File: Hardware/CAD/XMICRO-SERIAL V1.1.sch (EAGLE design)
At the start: 92 parts, among them J1 D9-MPH, J2 D9-MPH, J3 MINI-DIN6, J4 PINHD1X3, J5 PINHD1X3, Q1 2N5088, Q2 2N5088, Q3 2N5088, U1 555, U10 74280, U11 74273, U12 74164, U13 74164, U14 7474, U15 74244, U16 74244, U17 74240, U18 74280, U19 74165, U2 7486, U20 74165, U21 74244, U22 7404, U23 74245, U24 16550, U25 16550, U26 75185, U27 75185, U3 7410, U4 7404, U5 7474, U6 7474, U7 7408, U8 74138, U9 74138, Y1 1.8432MHz

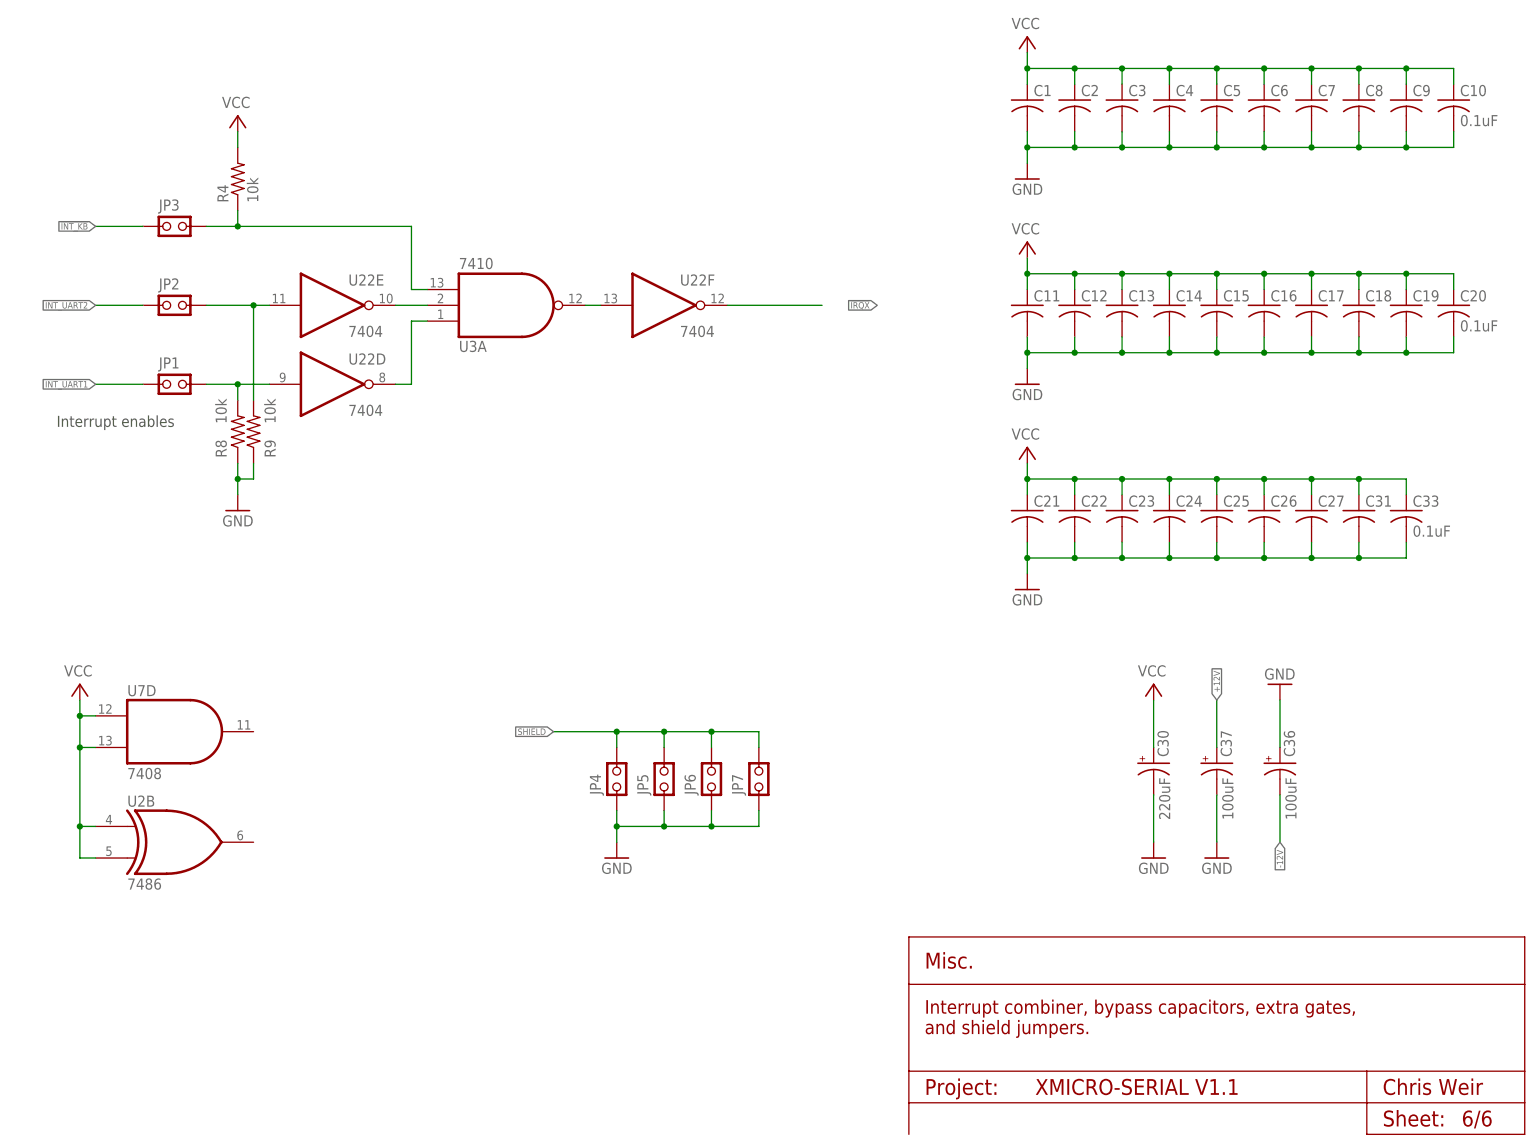
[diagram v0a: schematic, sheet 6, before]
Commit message: Updated design to V1.1 - added Schmitt trigger inputs, improved connector spacing, fixed PS/2 connector footprint
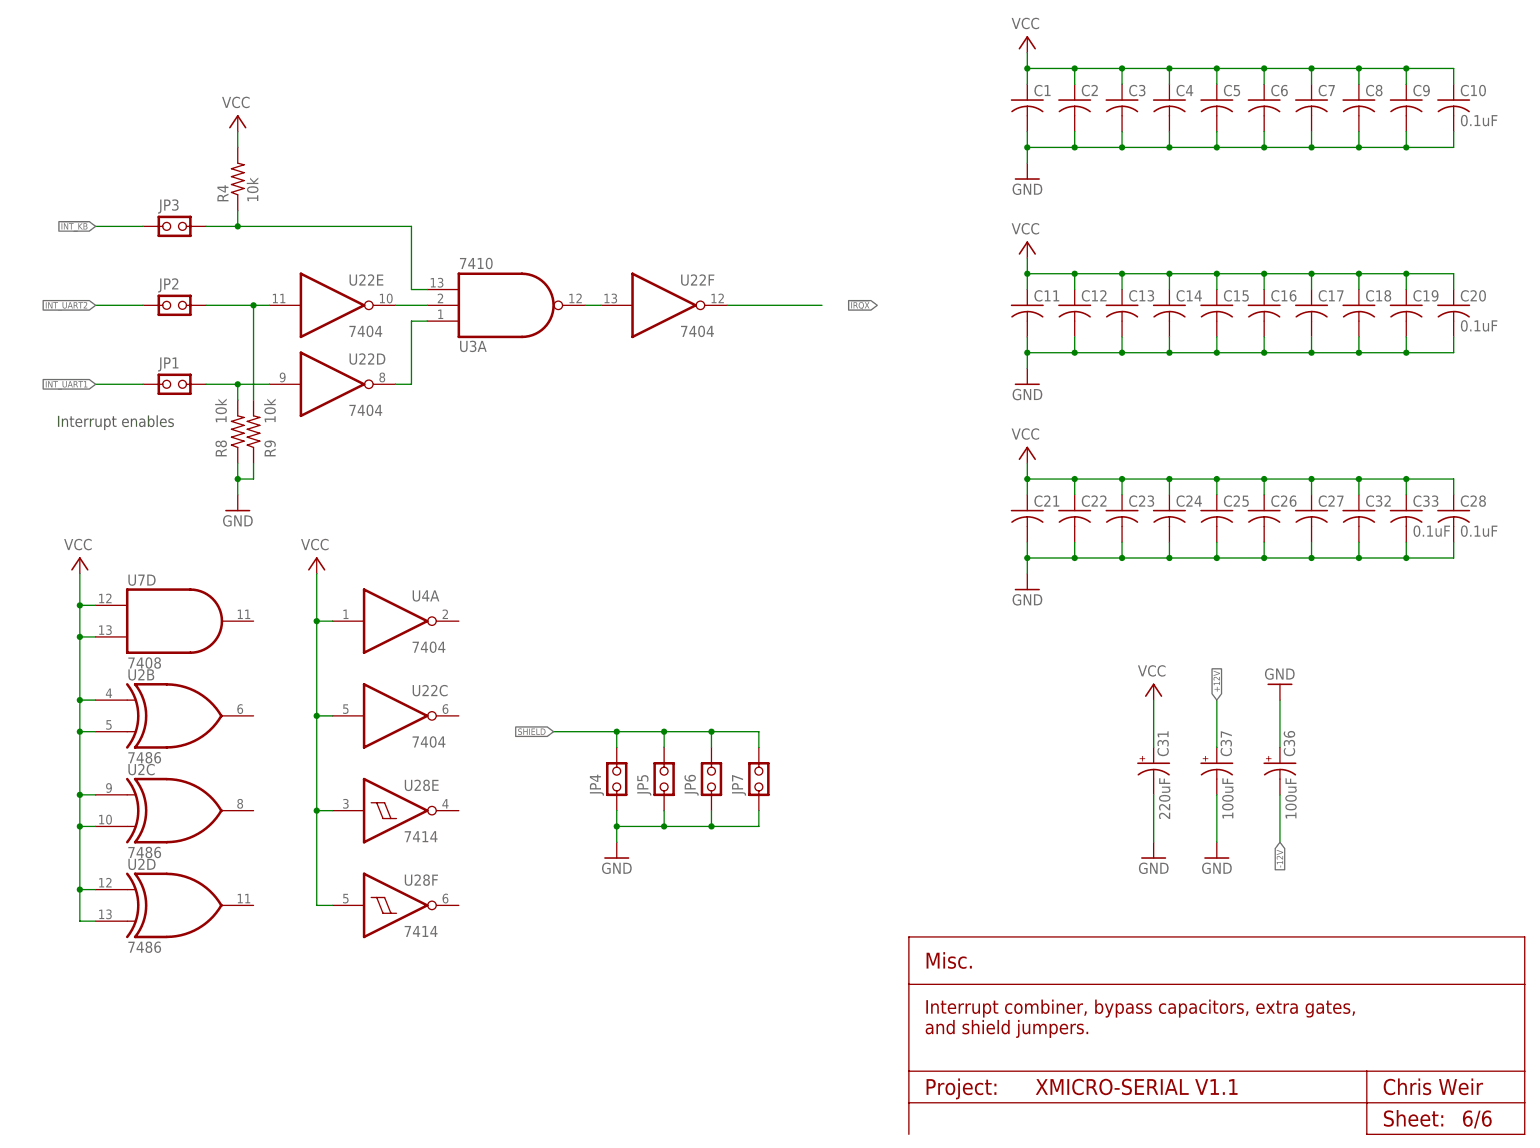
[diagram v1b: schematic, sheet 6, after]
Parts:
- added C32: 0.1uF, Custom:C-US100
- added U28: 7414, 74xx-us:74LS14N
- C28: value 10nF -> 0.1uF
- C29: value 0.1uF -> 10nF; device rcl:CPOL-USE2.5-6 -> Custom:C-US100
- C30: value 220uF -> 0.1uF; device Custom:CPOL-US-10-5 -> rcl:CPOL-USE2.5-6
- C31: value 0.1uF -> 220uF; device Custom:C-US100 -> Custom:CPOL-US-10-5
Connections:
- removed net N$26: U22C.O, U24G$1.RESET, U25G$1.RESET
- new net RST: U24G$1.RESET, U25G$1.RESET, U28C.O, U28D.I
- net !BRST: now also U28C.I; no longer U2D.I1
- net !KB_DATA: now also U28A.O; no longer U4A.O
- net !RST: now also U28D.O; no longer U22C.I, U2D.O
- net BUFF_KB_CLOCK: now also U28B.O; no longer U2C.O
- net GND: now also C29.2, C31.-, C32.2, U8P.GND; no longer C29.-, C31.2, U2C.I1, U2D.I0
- net KB_CLOCK: now also U28B.I; no longer U2C.I0
- net KB_DATA: now also U28A.I; no longer U4A.I
- net N$133: now also C30.+; no longer C29.+
- net N$140: now also C29.1; no longer C28.1
- net VCC: now also C28.1, C31.+, C32.1, U22C.I, U28E.I, U28F.I, U2C.I0, U2C.I1, U2D.I0, U2D.I1, U4A.I, U8P.VCC; no longer C30.+, C31.1
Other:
- moved on the sheet: U2B, U7D

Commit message: Fixed a schematic issue - added second inverter to BUFF_KB_CLOCK signal.
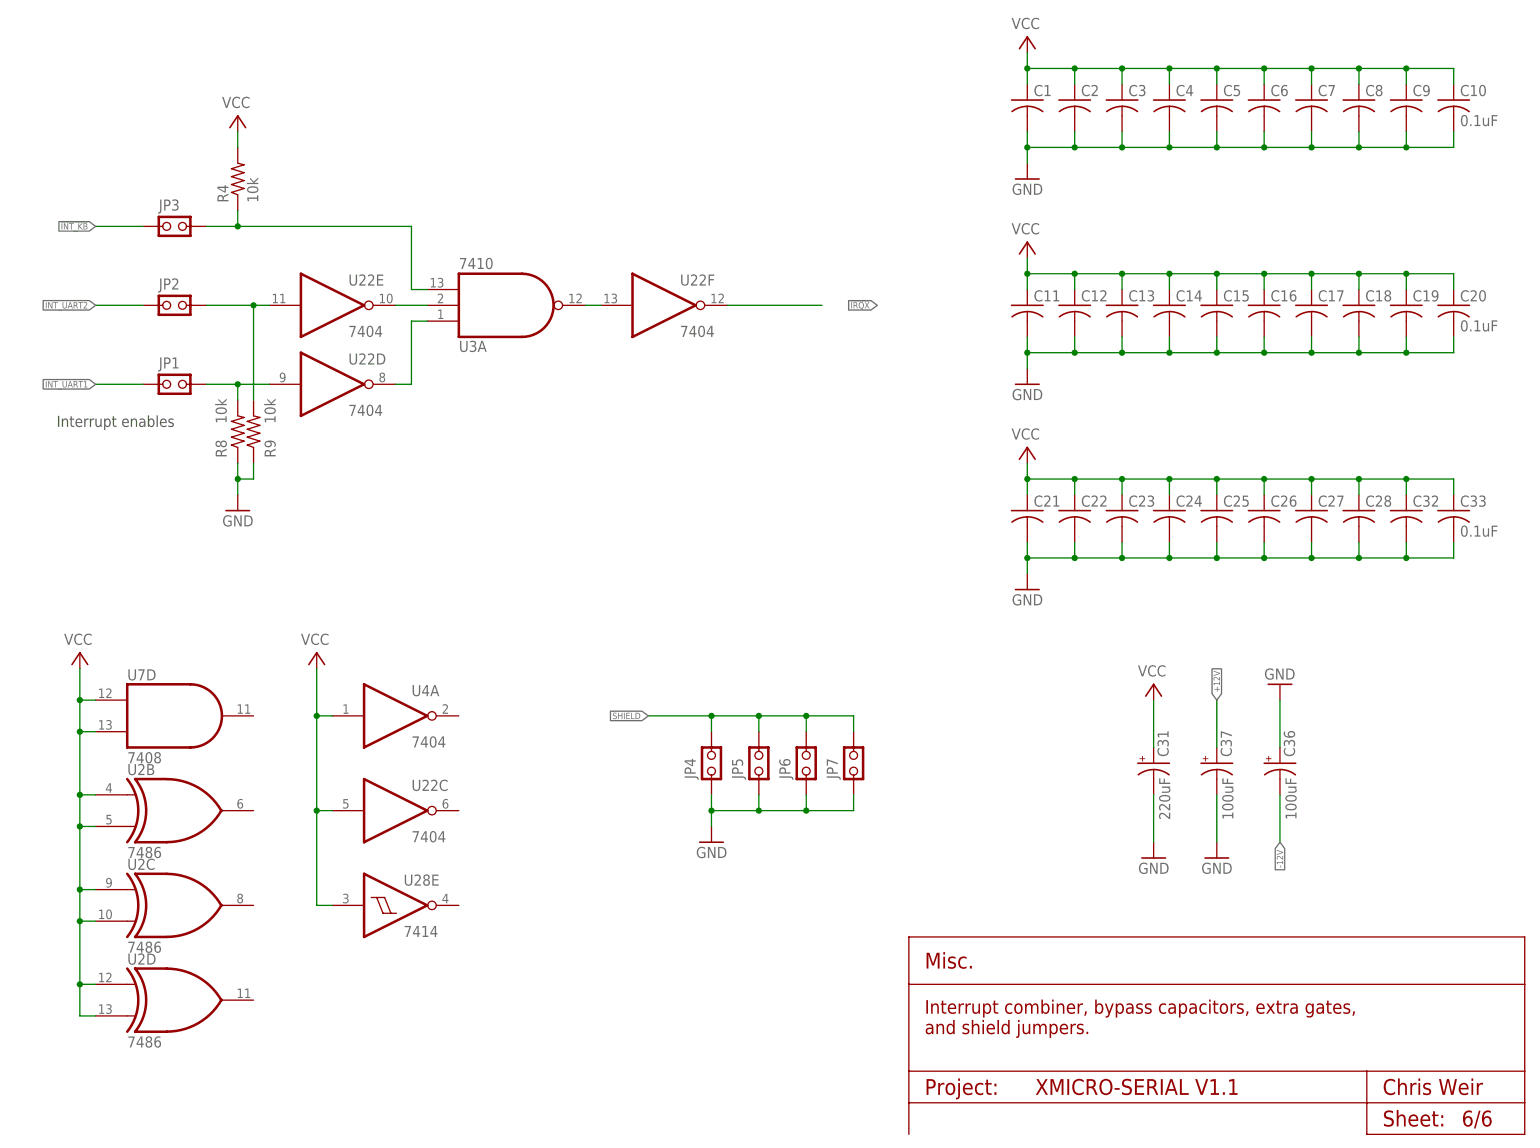
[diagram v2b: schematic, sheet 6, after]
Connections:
- new net N$26: U28B.O, U28C.I
- net !BRST: now also U28F.I; no longer U28C.I
- net BUFF_KB_CLOCK: now also U28C.O; no longer U28B.O
- net RST: now also U28F.O; no longer U28C.O
- net VCC: no longer U28F.I
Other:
- moved on the sheet: C28, C32, C33, JP4, JP5, JP6, JP7, U22C, U28E, U2B, U2C, U2D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

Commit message: Updated to hardware V1.1.
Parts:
- removed C35: 0.1uF, Custom:C-US100
- removed C36, C37: 100uF, rcl:CPOL-USE2.5-7
- added C38, C39: 10uF, rcl:CPOL-USE2.5-5
- added C40: 0.1uF, Custom:C-US100
- added U29: TC962, Custom:TC962
- C34: value 0.1uF -> 10uF; device Custom:C-US100 -> rcl:CPOL-USE2.5-5
- RN1: device resistor-sil:G08R -> Custom:RN8; OC_FARNELL unknown -> (none); OC_NEWARK unknown -> (none)
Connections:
- new net N$27: C38.-, U29.C-
- new net N$43: C38.+, U29.C+
- net +12V: now also C34.+, C40.1, U29.VDD; no longer C34.1, C35.1, C37.+
- net -12V: now also C39.-, U29.VOUT; no longer C34.2, C35.2, C36.-, CE0.-12V@7
- net GND: now also C34.-, C39.+, C40.2, U29.GND; no longer C36.+, C37.-
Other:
- note added: "XMICRO bus interface. Buffers provide isolation and reduced loading on bus lines. U29 supplies -12V to the RS232 transcievers."
- note removed: "XMICRO bus interface. Buffers provide isolation and reduced loading on bus lines."
- moved on the sheet: C31
